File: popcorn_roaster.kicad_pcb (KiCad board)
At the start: 2 copper layers, 105.8 x 77.9 mm, 38 parts, among them Q1 BC847B, U1 R-78K3.3-0.5, U2 IRM-45-24, U3 MOC3063S, U4 MAX31855

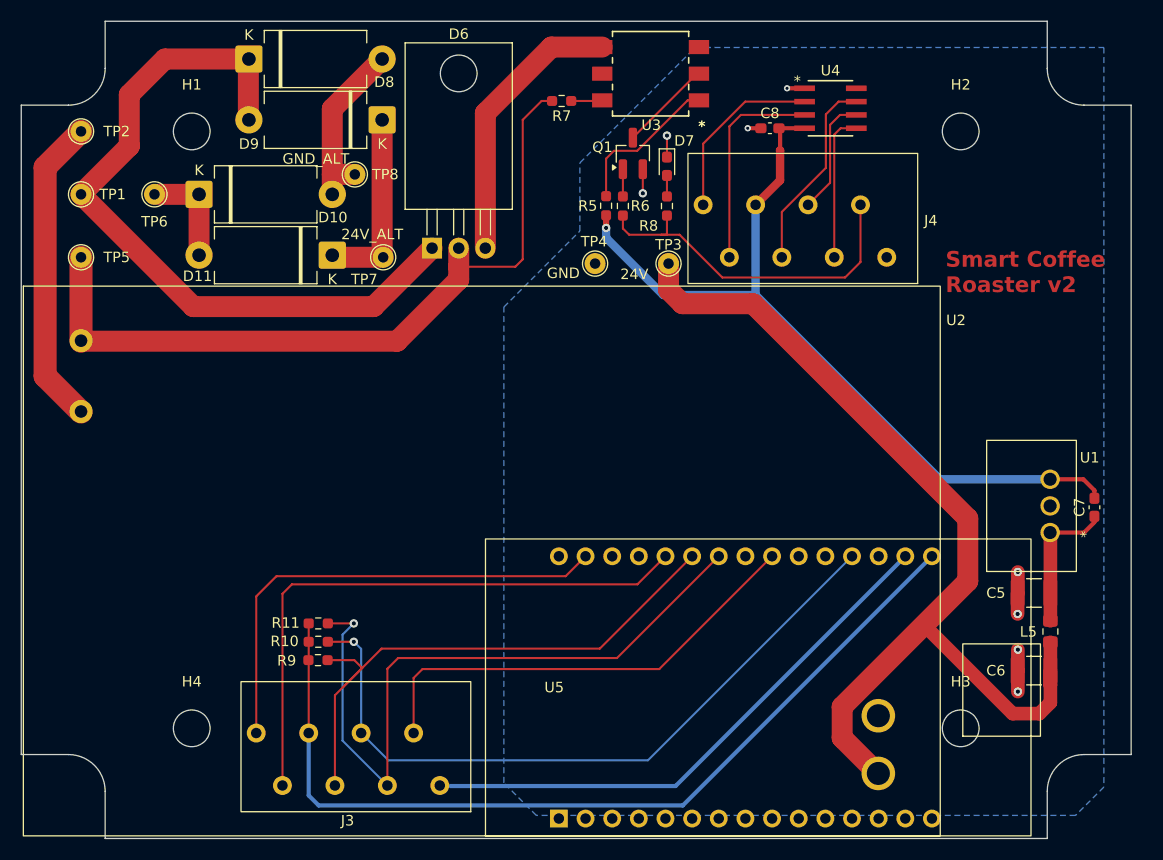
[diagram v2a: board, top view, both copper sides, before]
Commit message: Change order of 8-pin terminal block pins
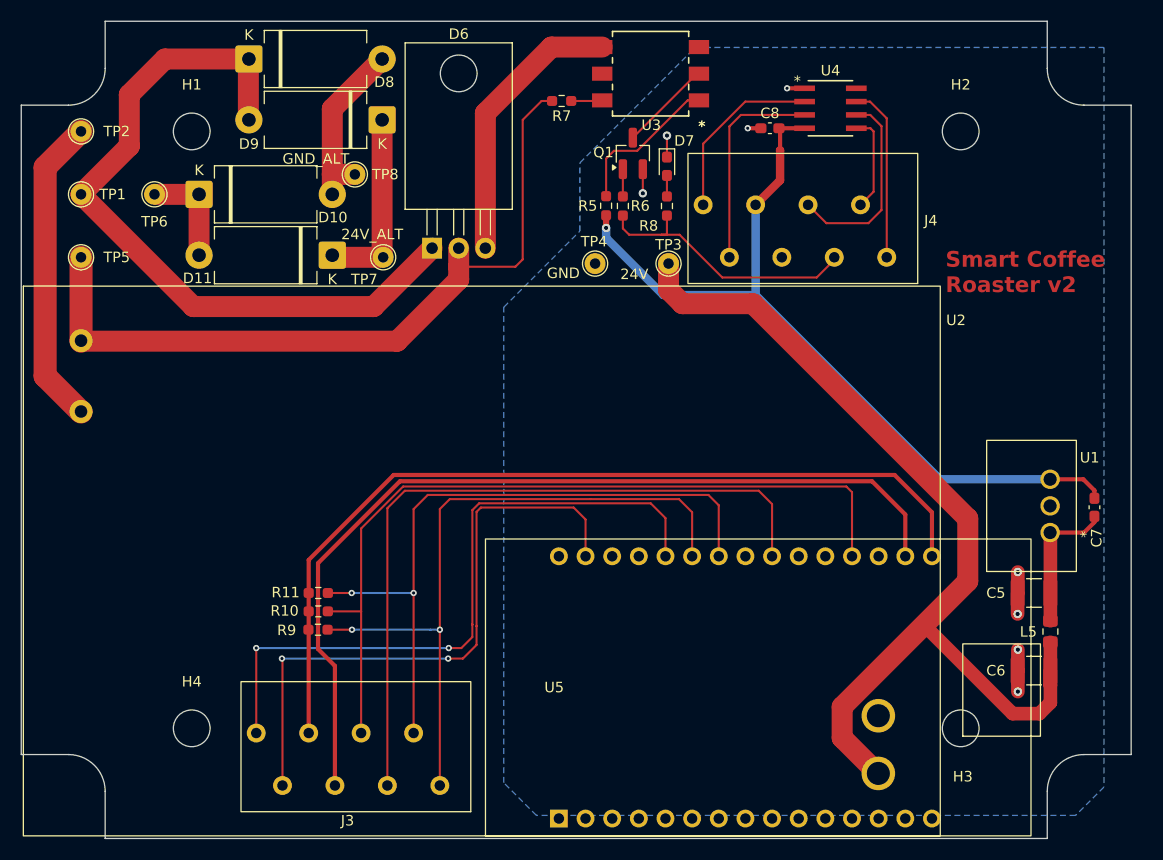
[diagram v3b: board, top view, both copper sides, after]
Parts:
- moved R10 2.90 mm to (28.3, 56.2)
- moved R11 2.90 mm to (28.3, 54.5)
- moved R9 2.90 mm to (28.3, 58.0)
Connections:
- J3 pad 1: Net-(J3-Pin_1) -> /Smart Roaster/RESERVED1_mc
- J3 pad 2: Net-(J3-Pin_2) -> /Smart Roaster/RESERVED2_mc
- J3 pad 4: /Smart Roaster/POCI_mc -> GND_mc
- J3 pad 6: /Smart Roaster/SCK_mc -> /Smart Roaster/HEAT_ON_mc
- J3 pad 7: /Smart Roaster/HEAT_ON_mc -> /Smart Roaster/SCK_mc
- J3 pad 8: GND_mc -> /Smart Roaster/POCI_mc
- J4 pad 4: /Smart Roaster/POCI -> GND
- J4 pad 6: /Smart Roaster/SCK -> /Smart Roaster/HEAT_ON
- J4 pad 7: /Smart Roaster/HEAT_ON -> /Smart Roaster/SCK
- J4 pad 8: GND -> /Smart Roaster/POCI
- U5 pad 26: Net-(J3-Pin_2) -> /Smart Roaster/RESERVED1_mc
- U5 pad 29: Net-(J3-Pin_1) -> /Smart Roaster/RESERVED2_mc
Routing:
- net /Smart Roaster/RESERVED1_mc: track 0.00 -> 64.1 mm, vias 0 -> 2
- net /Smart Roaster/RESERVED2_mc: track 0.00 -> 58.6 mm, vias 0 -> 2
- net Net-(J3-Pin_2): track 56.3 -> 0.00 mm
- net Net-(J3-Pin_1): track 46.0 -> 0.00 mm
- net GND_mc: track 52.4 -> 86.4 mm
- net /Smart Roaster/HEAT_ON_mc: track 44.2 -> 69.3 mm
- net /Smart Roaster/POCI_mc: track 54.3 -> 66.3 mm, vias 0 -> 2
- net /Smart Roaster/nCS_mc: track 67.4 -> 77.5 mm, vias 1 -> 0
- net /Smart Roaster/HEAT_ON: track 34.2 -> 26.0 mm
- net /Smart Roaster/nCS: track 11.4 -> 19.1 mm
- net /Smart Roaster/SCK: track 14.0 -> 9.29 mm
- net /Smart Roaster/SCK_mc: track 67.3 -> 64.4 mm, vias 1 -> 2
- net /Smart Roaster/POCI: track 18.8 -> 16.8 mm
- net +3V3_mc: track 86.0 -> 84.9 mm

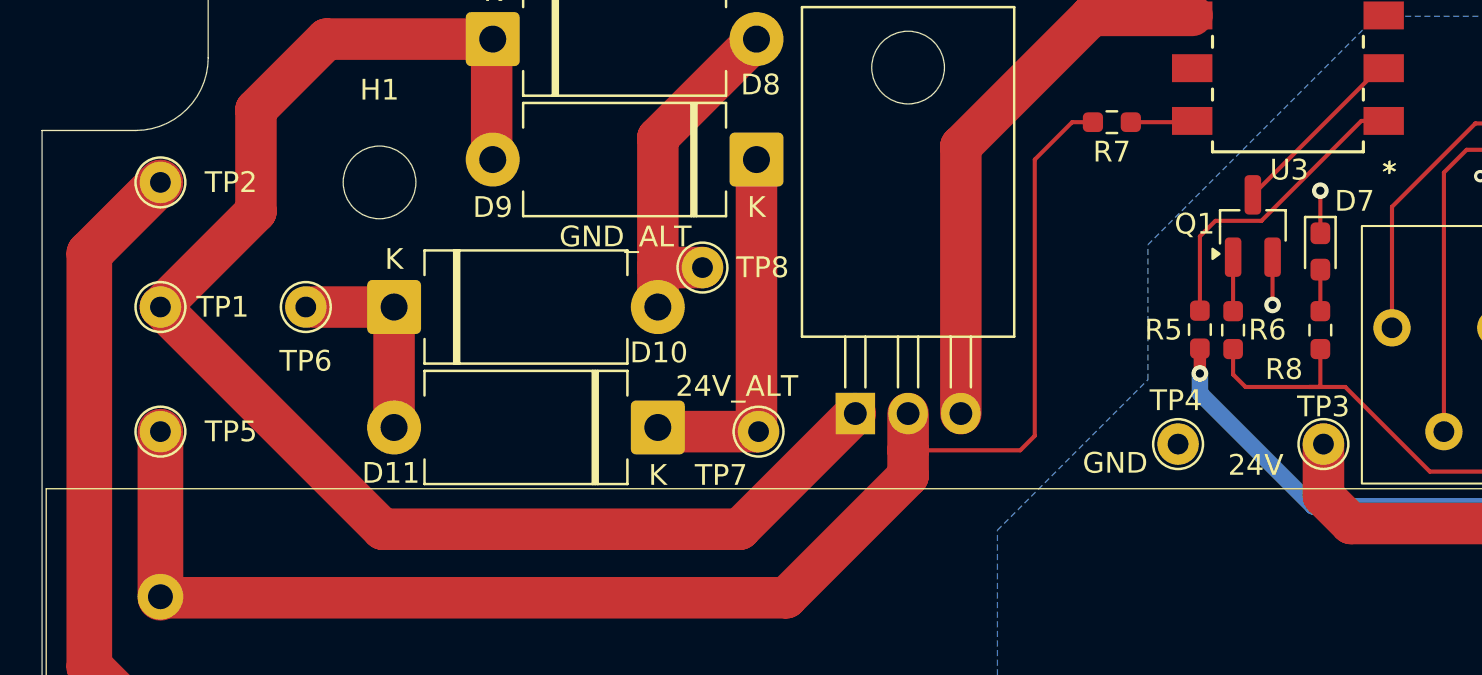
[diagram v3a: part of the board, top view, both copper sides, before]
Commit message: Make test point holes larger (1.0 => 1.5 mm)
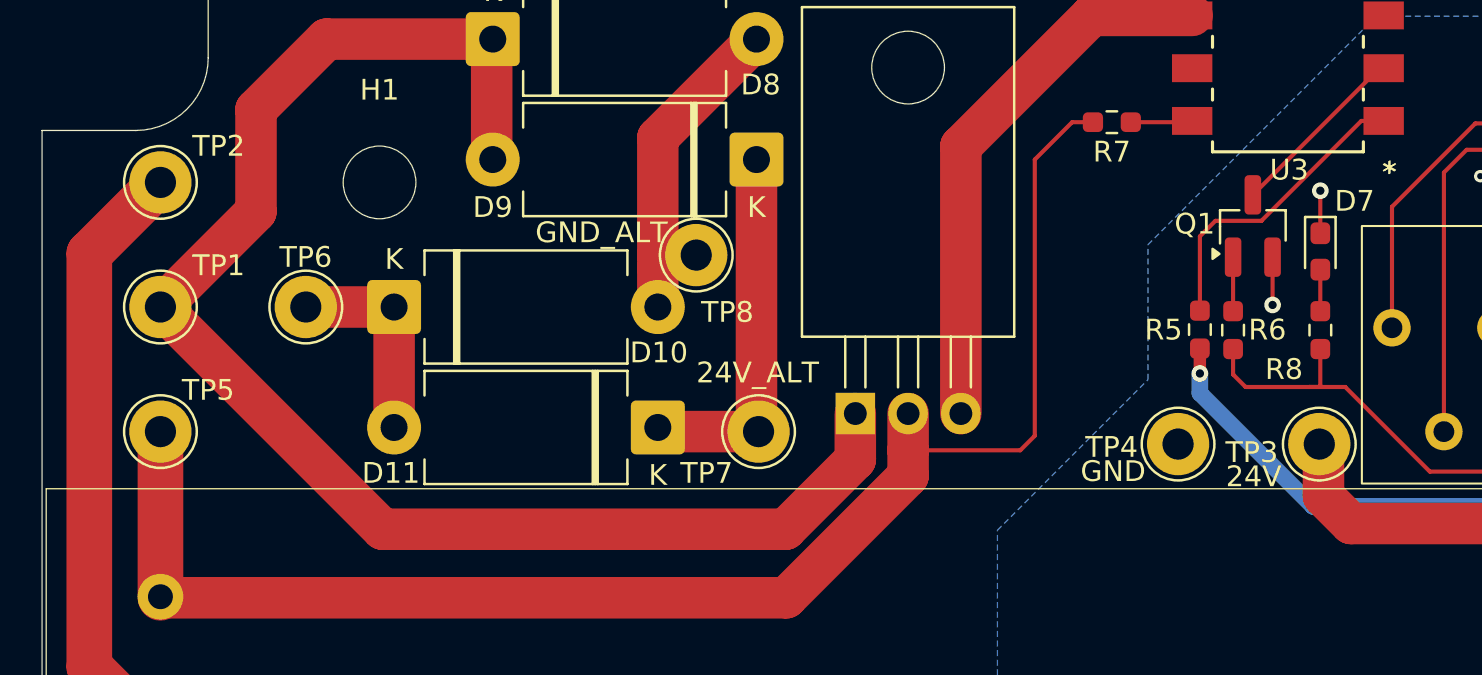
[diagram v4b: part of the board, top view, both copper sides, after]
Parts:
- TP1, TP2, TP3, TP4, TP5, TP6, TP7, TP8: footprint TestPoint:TestPoint_THTPad_D2.0mm_Drill1.0mm -> TestPoint:TestPoint_THTPad_D3.0mm_Drill1.5mm
- moved TP8 0.67 mm to (31.5, 14.0)
- moved TP3 0.20 mm to (61.5, 23.1)
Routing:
- net /Smart Roaster/heat_blue: track 70.2 -> 71.5 mm
